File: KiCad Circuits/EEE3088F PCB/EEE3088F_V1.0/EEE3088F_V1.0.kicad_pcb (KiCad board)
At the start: 2 copper layers, 60 parts, among them J1 Conn_01x02_Pin, J2 Conn_02x16_Odd_Even, U1 MT3608, U10 HX SS12D10G6-WJ, U11 HUSB237-AA001-DN06R, U2 INA219AxD, U3 DRV8833PWP, U4 AP2112K-3.3, U5 DRV8833PWP, U6 BQ24074RGT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

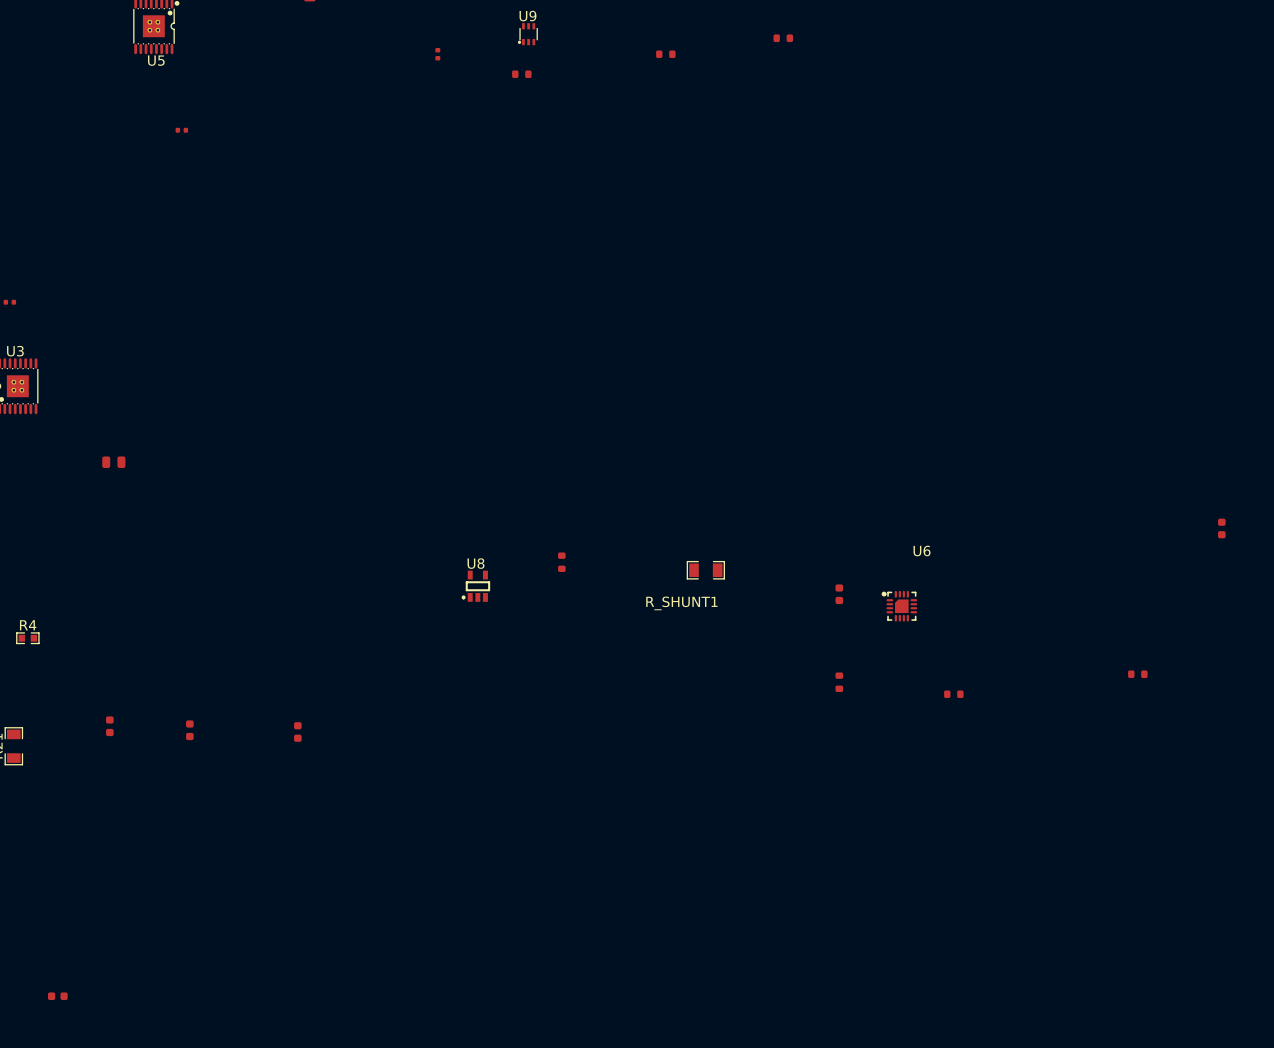
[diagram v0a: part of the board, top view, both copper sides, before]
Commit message: Updated components, started PCB
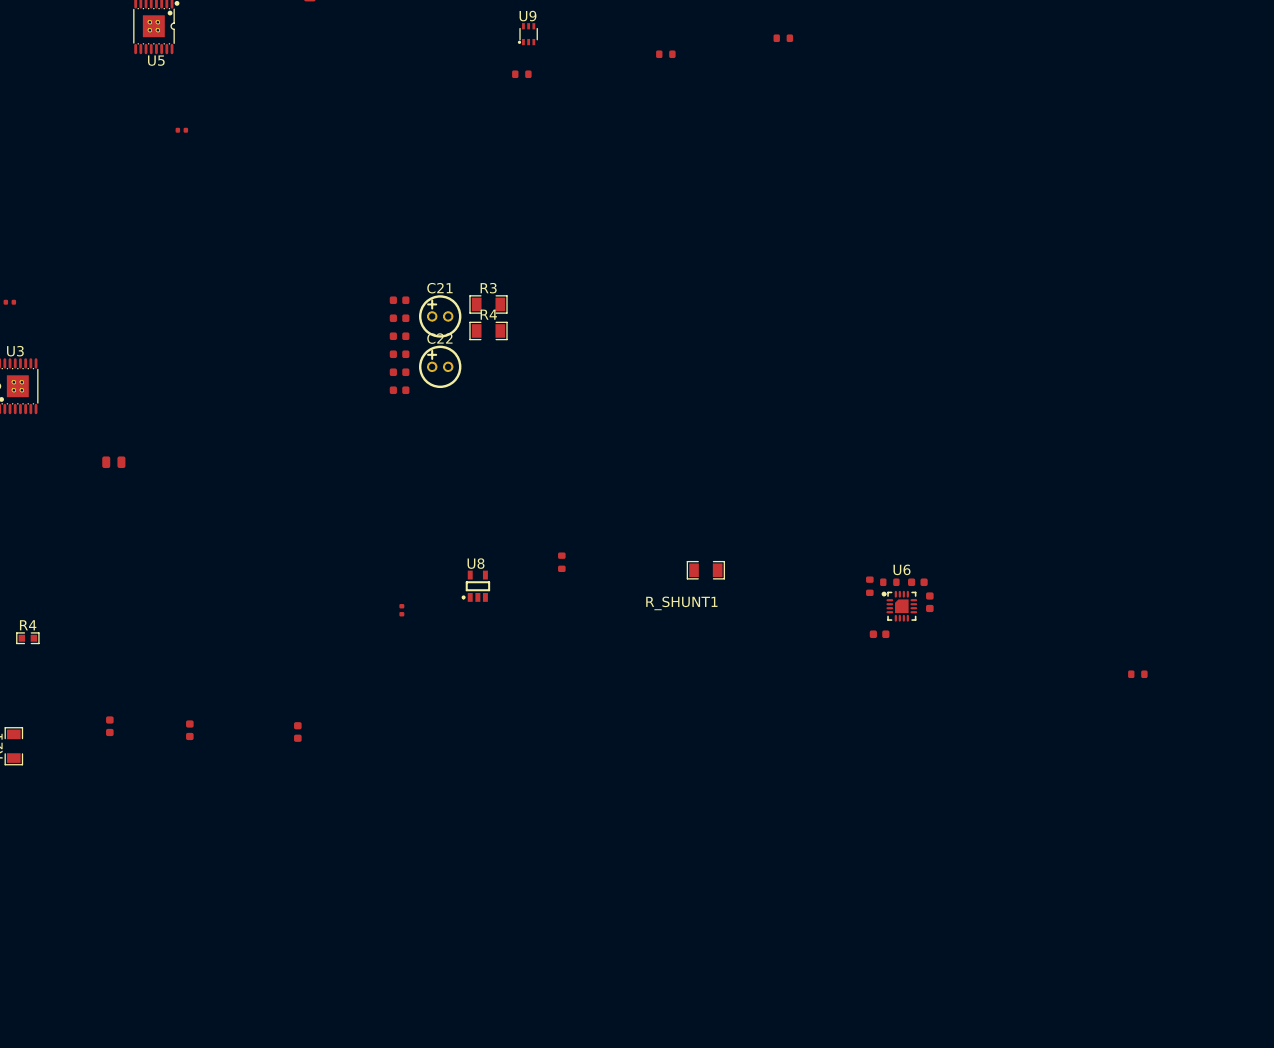
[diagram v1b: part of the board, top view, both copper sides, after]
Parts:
- added C15: 4.7uF, PCM_JLCPCB:C_0603, F.Cu at (101.7, 84.8)
- added C16: 4.7uF, PCM_JLCPCB:C_0603, F.Cu at (101.7, 87.0)
- added C2: 1uF, PCM_JLCPCB:C_0603, F.Cu at (101.7, 75.8)
- added C21: 10uF, Footprints:CAP-TH_BD5.0-P2.00-D0.8-FD, F.Cu at (106.8, 77.8)
- added C22: 10uF, Footprints:CAP-TH_BD5.0-P2.00-D0.8-FD, F.Cu at (106.8, 84.1)
- added C3: 1uF, PCM_JLCPCB:C_0603, F.Cu at (101.7, 78.0)
- added C5: 1uF, PCM_JLCPCB:C_0603, F.Cu at (101.7, 80.2)
- added C6: 1uF, PCM_JLCPCB:C_0603, F.Cu at (101.7, 82.5)
- added R3: 430m, Footprints:R1206, F.Cu at (112.8, 76.3)
- added R4: 430m, Footprints:R1206, F.Cu at (112.8, 79.6)
- moved C4 119.6 mm to (168.0, 113.5), turned to 90 degrees
- moved C14 69.6 mm to (102.0, 114.5)
- moved C1 38.6 mm to (166.5, 111.0), turned to 180 degrees
- moved R10 16.1 mm to (163.0, 111.0)
- moved R6 12.6 mm to (160.5, 111.5), turned to 90 degrees
- moved C11 7.10 mm to (161.7, 117.5), turned to 0 degrees

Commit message: Pcb changes
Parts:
- moved U10 227.6 mm to (90.5, 252.3), turned to 0 degrees
- moved J2 213.8 mm to (110.7, 242.5), turned to -90 degrees
- moved R20 210.9 mm to (85.0, 234.5), turned to 90 degrees
- moved C20 209.8 mm to (240.0, 195.0)
- moved R17 209.8 mm to (233.5, 222.0)
- moved U4 209.8 mm to (147.5, 214.5)
- moved R14 208.1 mm to (113.5, 225.5)
- moved R13 206.0 mm to (107.0, 226.0)
- moved R16 202.7 mm to (68.7, 208.0), turned to 0 degrees
- moved R19 197.4 mm to (86.5, 230.0)
- moved U9 194.2 mm to (88.5, 234.5), turned to 180 degrees
- moved R18 190.4 mm to (90.0, 230.0), turned to 90 degrees
- moved U5 182.0 mm to (106.5, 220.0), turned to 0 degrees
- moved C9 177.5 mm to (108.5, 213.5), turned to 0 degrees
- moved C25 161.4 mm to (102.0, 213.5), turned to 180 degrees
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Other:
- board outline added: 60 x 82 mm

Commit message: Updated the Kicad pcb
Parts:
- moved C8 323.3 mm to (397.0, 163.7)
- moved C16 297.5 mm to (389.7, 144.5)
- moved C17 247.8 mm to (78.5, 217.0), turned to 180 degrees
- moved D1 246.4 mm to (107.2, 229.5), turned to -90 degrees
- moved C21 242.7 mm to (392.7, 124.0)
- moved R23 238.9 mm to (71.0, 225.5)
- moved USB1 238.7 mm to (64.8, 243.1), turned to 0 degrees
- moved R9 233.9 mm to (103.2, 232.0), turned to 180 degrees
- moved L1 233.0 mm to (106.7, 235.5)
- moved U7 230.1 mm to (74.5, 225.5)
- moved U1 222.1 mm to (103.2, 235.5), turned to 90 degrees
- moved R5 219.5 mm to (100.7, 233.0), turned to 90 degrees
- moved U11 215.7 mm to (64.3, 237.0)
- moved C12 208.6 mm to (95.0, 224.0), turned to 180 degrees
- moved R22 207.7 mm to (60.5, 234.5), turned to 90 degrees
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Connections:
- U11 pad 2: Net-(U11-VUSB) -> HV
- USB1 pad A9: Net-(U11-VUSB) -> HV
- USB1 pad B9: Net-(U11-VUSB) -> HV

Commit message: Component position complete
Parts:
- removed the C16 at (389.7, 144.5)
- removed the C2 at (103.2, 230.0)
- removed the C21 at (392.7, 124.0)
- removed the C3 at (103.2, 239.0)
- removed the C5 at (400.5, 171.5)
- removed the C6 at (111.2, 232.0)
- removed C7, C8: 10uF, PCM_JLCPCB:C_0603
- removed R11, R21: 0.25, Footprints:R1206
- removed the R3 at (25.5, 119.2)
- removed the R4 at (55.3, 118.0)
- C19: value 10uF -> 1uF
- moved C19 332.0 mm to (61.5, 235.5)
- moved C3 159.1 mm to (95.0, 237.0), turned to 90 degrees
- moved C5 158.9 mm to (107.5, 239.0), turned to 180 degrees
- moved C2 156.3 mm to (98.5, 232.0), turned to 180 degrees
- moved R17 151.5 mm to (82.0, 217.5)
- moved C6 150.6 mm to (107.5, 233.0), turned to 180 degrees
- moved R3 149.4 mm to (65.5, 218.0), turned to -90 degrees
- moved R4 137.1 mm to (70.5, 210.0), turned to 180 degrees
- moved U9 114.5 mm to (84.0, 214.5), turned to 0 degrees
- moved C9 108.2 mm to (103.3, 210.5), turned to 90 degrees
- moved R20 107.3 mm to (87.5, 212.0), turned to 0 degrees
- moved C26 106.1 mm to (76.5, 213.5)
- moved U3 105.7 mm to (70.5, 214.5)
- moved C15 105.2 mm to (103.5, 214.5), turned to -90 degrees
- moved R18 104.5 mm to (87.5, 215.0), turned to -90 degrees
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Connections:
- C19 pad 1: Net-(U11-VUSB) -> HV

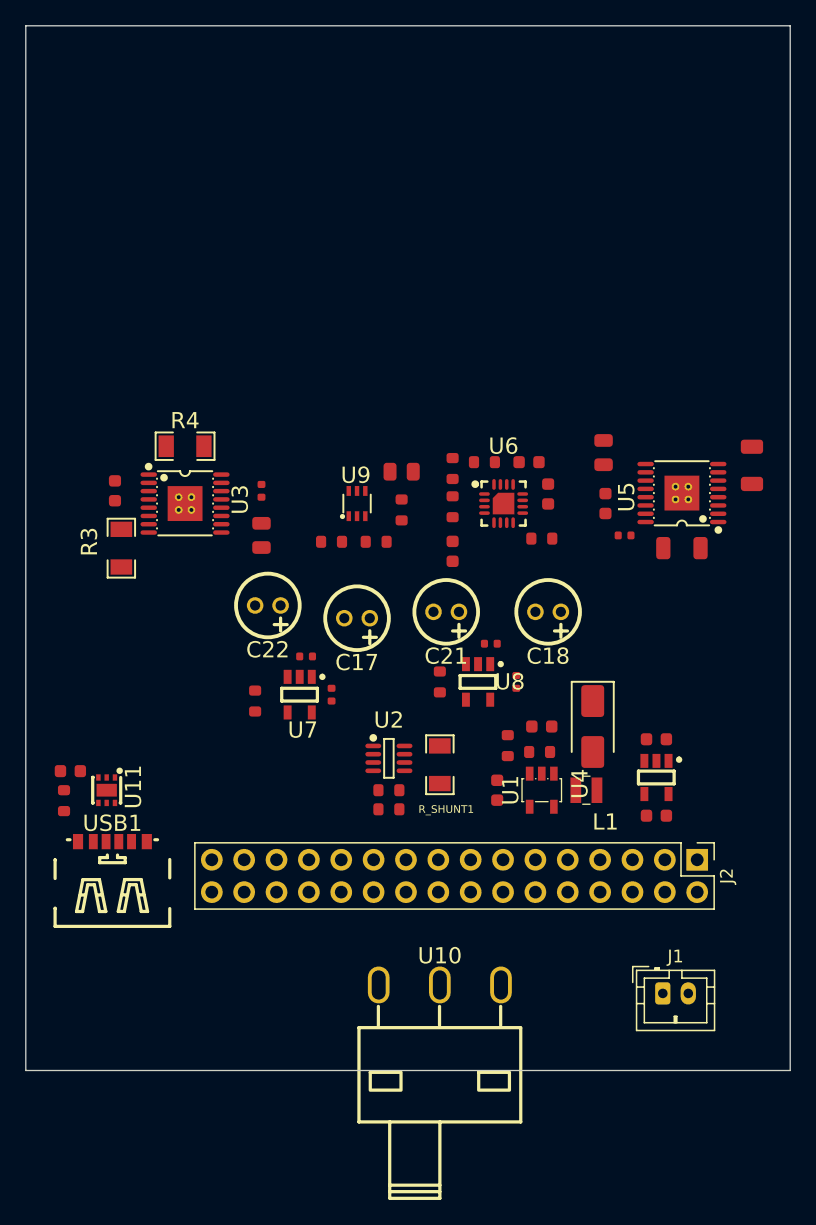
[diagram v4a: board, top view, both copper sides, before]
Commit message: PCB connected but not error free
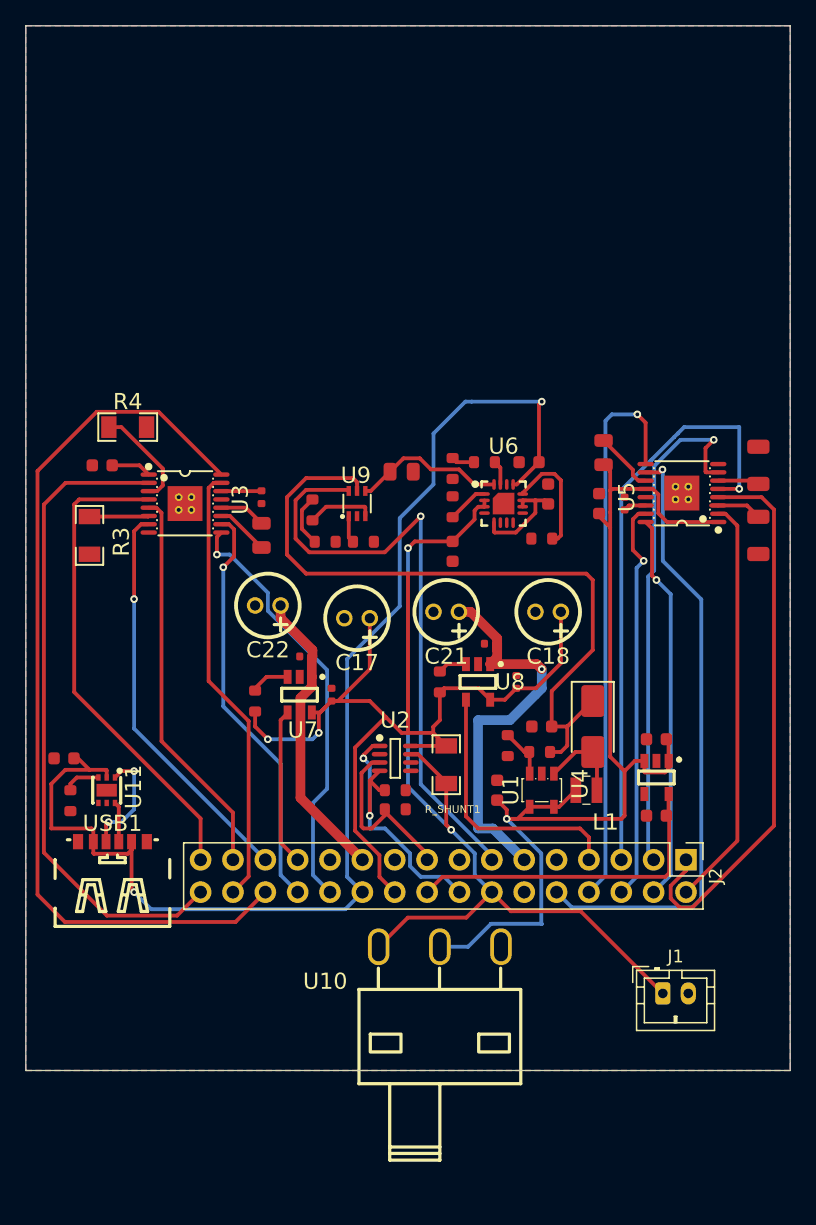
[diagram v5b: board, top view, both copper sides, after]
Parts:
- moved R18 7.00 mm to (80.5, 215.0), turned to 90 degrees
- moved R13 6.08 mm to (115.5, 217.0), turned to 90 degrees
- moved R4 4.74 mm to (66.0, 208.5)
- moved R19 4.00 mm to (81.5, 217.5), turned to 180 degrees
- moved U10 3.00 mm to (90.5, 249.3)
- moved R3 2.69 mm to (63.0, 217.0), turned to 90 degrees
- moved C25 2.50 mm to (105.0, 214.5), turned to -90 degrees
- moved R17 2.50 mm to (84.5, 217.5)
- moved C16 2.24 mm to (64.0, 211.5), turned to 180 degrees
- moved C19 1.12 mm to (61.0, 234.5)
- moved J2 0.88 mm to (109.8, 242.5)
- moved C15 0.50 mm to (103.0, 214.5), turned to 90 degrees
- moved C26 0.50 mm to (76.5, 214.0)
- moved R1 0.50 mm to (87.0, 238.5)
- moved R14 0.50 mm to (115.5, 211.5)
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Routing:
- net 5V Out: track 0.00 -> 135.3 mm, vias 0 -> 2
- net HV: track 0.00 -> 98.9 mm, vias 0 -> 2
- net Battery Out: track 0.00 -> 89.8 mm, vias 0 -> 1
- net Battery: track 0.00 -> 73.0 mm, vias 0 -> 2
- net MOTOR1_CTRL1: track 0.00 -> 71.4 mm
- net MOTOR1_A_OUT: track 0.00 -> 51.4 mm
- net FAST_CHARGE_CTRL: track 0.00 -> 48.9 mm, vias 0 -> 1
- net MOTOR4_CTRL2: track 0.00 -> 48.5 mm, vias 0 -> 1
- net MOTOR4_B_OUT: track 0.00 -> 46.8 mm, vias 0 -> 1
- net MOTOR4_CTRL1: track 0.00 -> 44.4 mm, vias 0 -> 1
- net MOTOR2_B_OUT: track 0.00 -> 44.2 mm
- net MOTOR4_A_OUT: track 0.00 -> 40.6 mm, vias 0 -> 1
- net MOTOR1_B_OUT: track 0.00 -> 38.0 mm
- net MOTOR1_CTRL2: track 0.00 -> 34.7 mm
- net MOTOR3_CTRL1: track 0.00 -> 33.6 mm, vias 0 -> 1
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- added copper zone on B.Cu, net GND
- added copper zone on F.Cu, net GND

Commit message: Edited Kicad
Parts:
- U1: footprint Footprints:SOT-23-5_L3.0-W1.7-P0.95-LS2.8-BR -> PCM_JLCPCB:SOT-23-5_L3.0-W1.7-P0.95-LS2.8-BR
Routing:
- net MOTOR4_CTRL1: track 44.4 -> 47.1 mm
- net MOTOR4_B_OUT: track 46.8 -> 47.7 mm

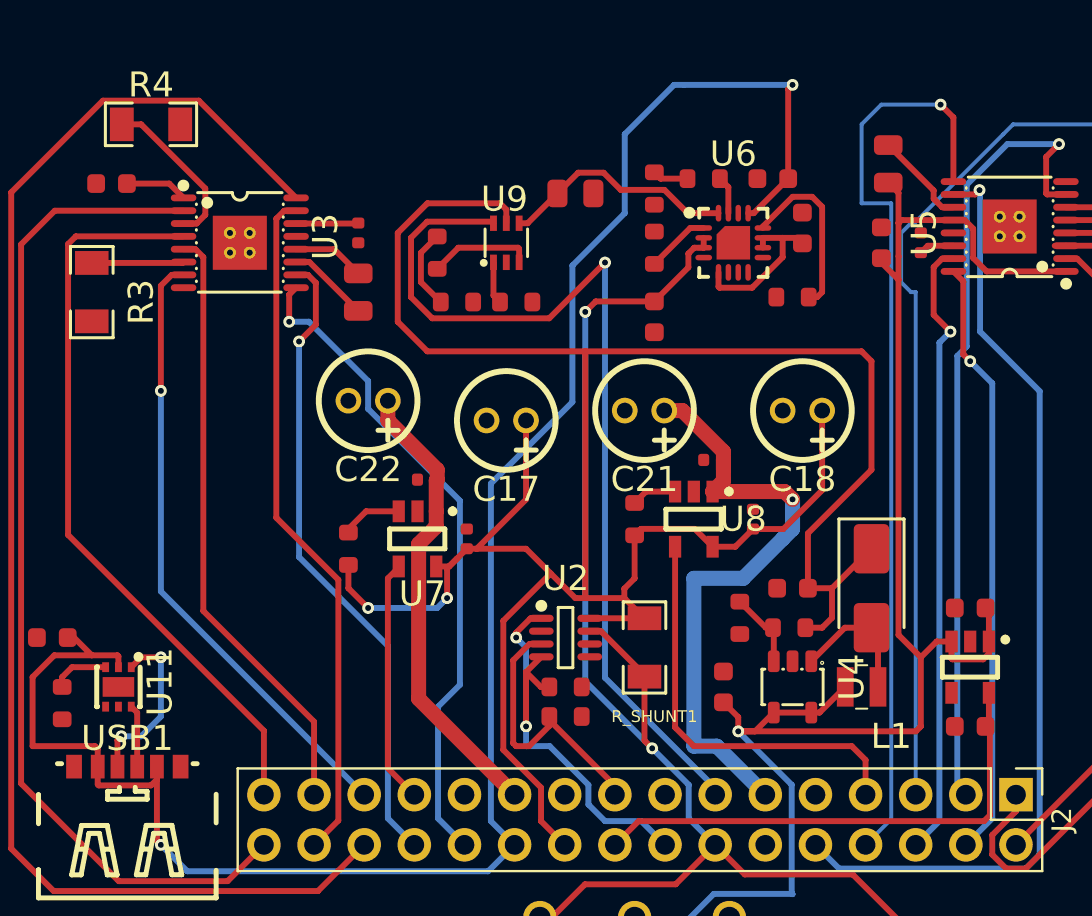
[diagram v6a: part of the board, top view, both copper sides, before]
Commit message: Updated pcb (missing connections)
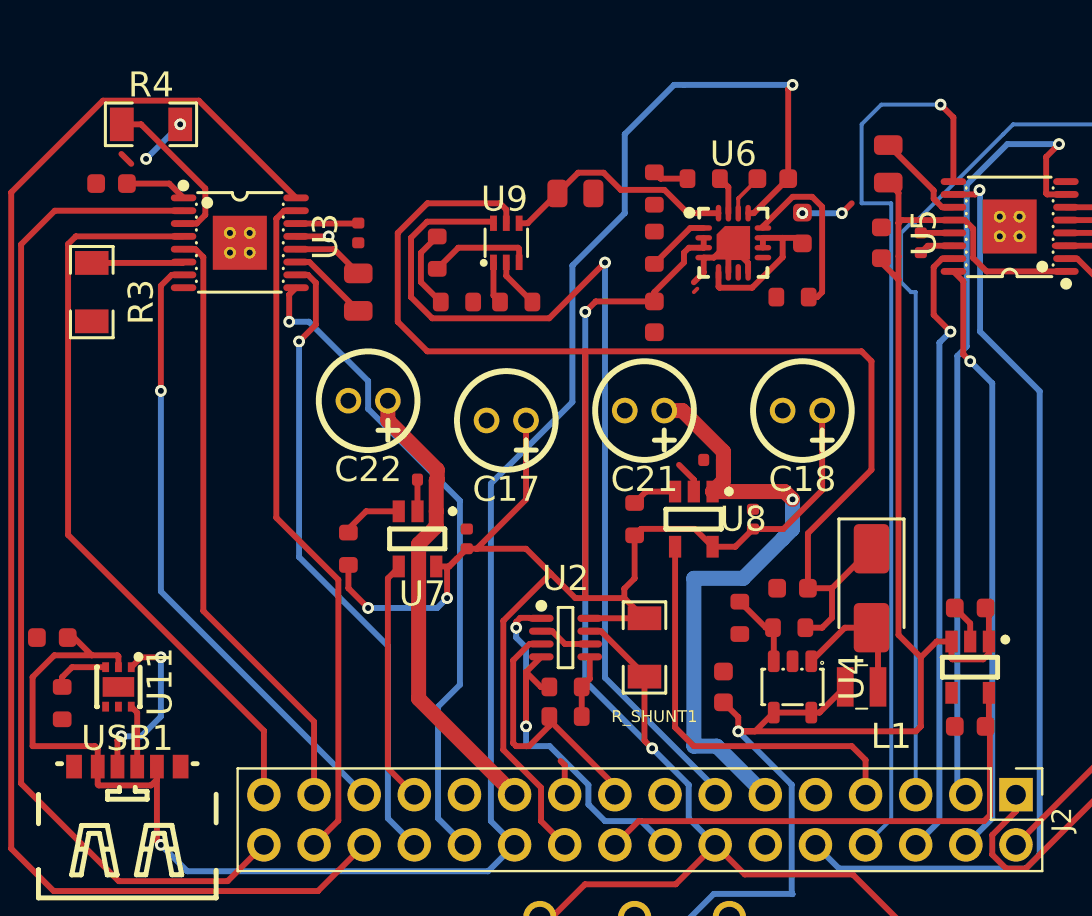
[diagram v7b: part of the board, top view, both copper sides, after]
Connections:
- U3 pad : (no net) -> GND
- U5 pad : (no net) -> GND
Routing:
- net GND: track 0.00 -> 29.8 mm, vias 0 -> 5
- net 3.3V Out: track 0.00 -> 3.19 mm

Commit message: Fixed pcb
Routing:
- net GND: track 29.8 -> 215.1 mm, vias 5 -> 8
- net Battery Out: track 89.8 -> 141.1 mm, vias 1 -> 4
- net FAST_CHARGE_CTRL: track 48.9 -> 49.9 mm
- net EXT_LOAD2_OUT: track 31.5 -> 32.2 mm
- net 5V Out: track 135.3 -> 136.0 mm
